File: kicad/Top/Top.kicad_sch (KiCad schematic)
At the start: 0 parts

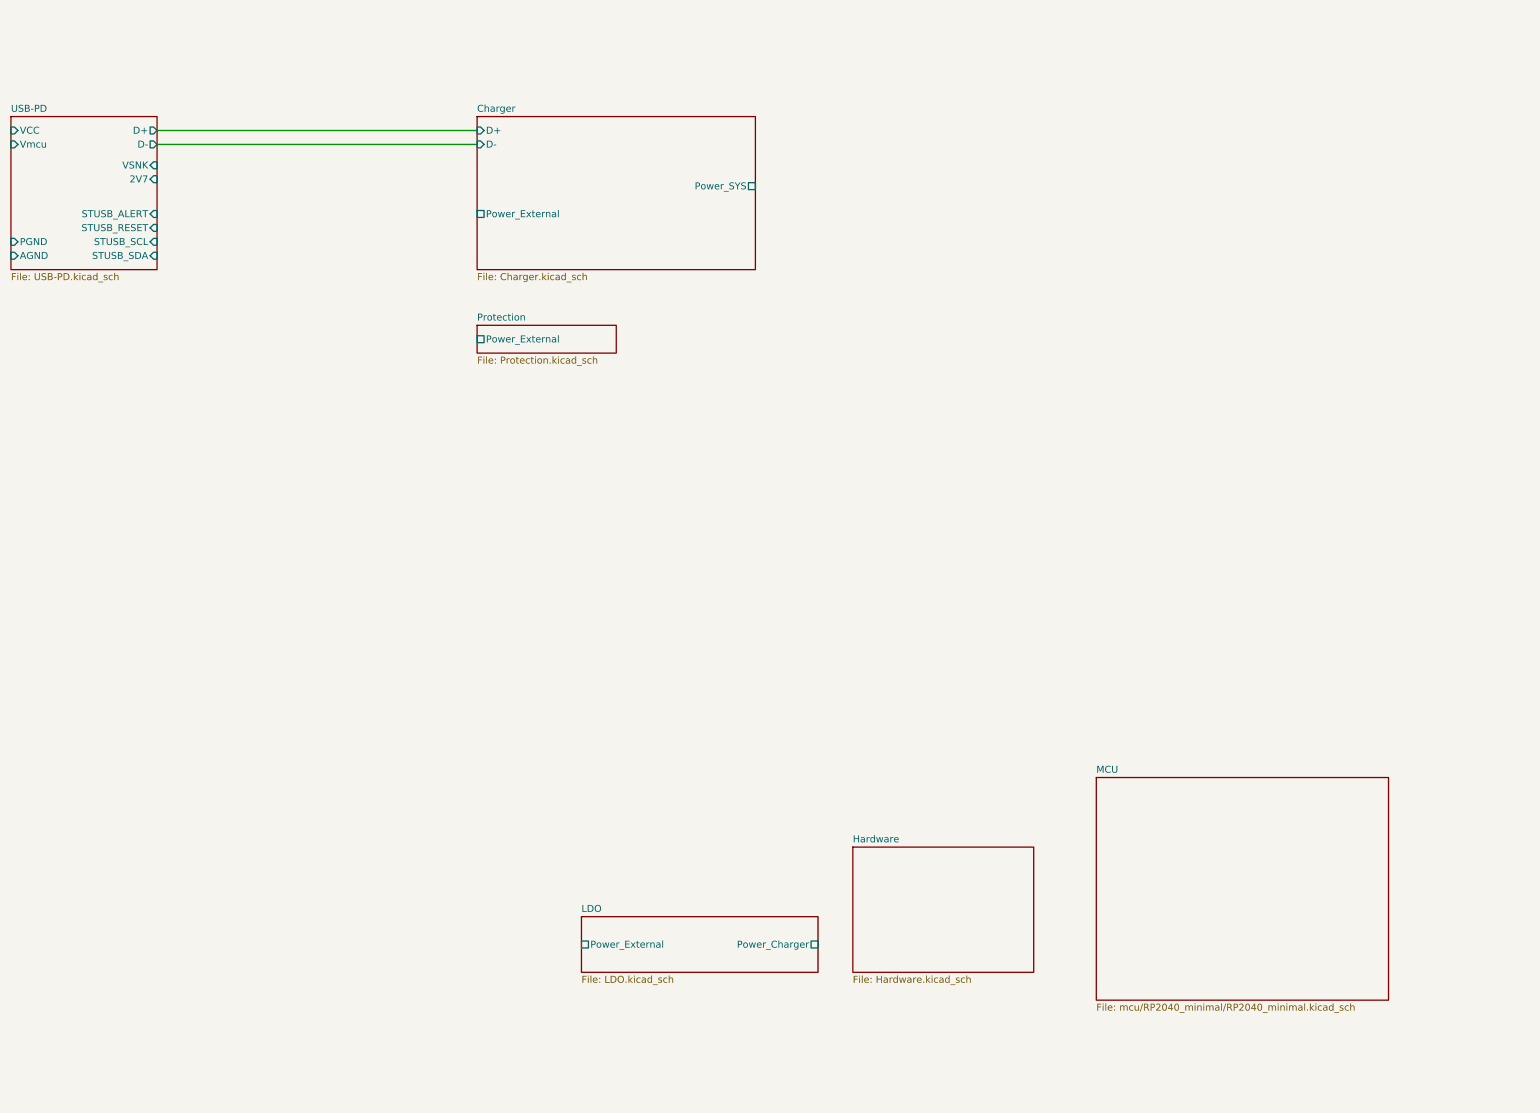
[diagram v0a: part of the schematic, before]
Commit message: Added hierarchial pins to mcu
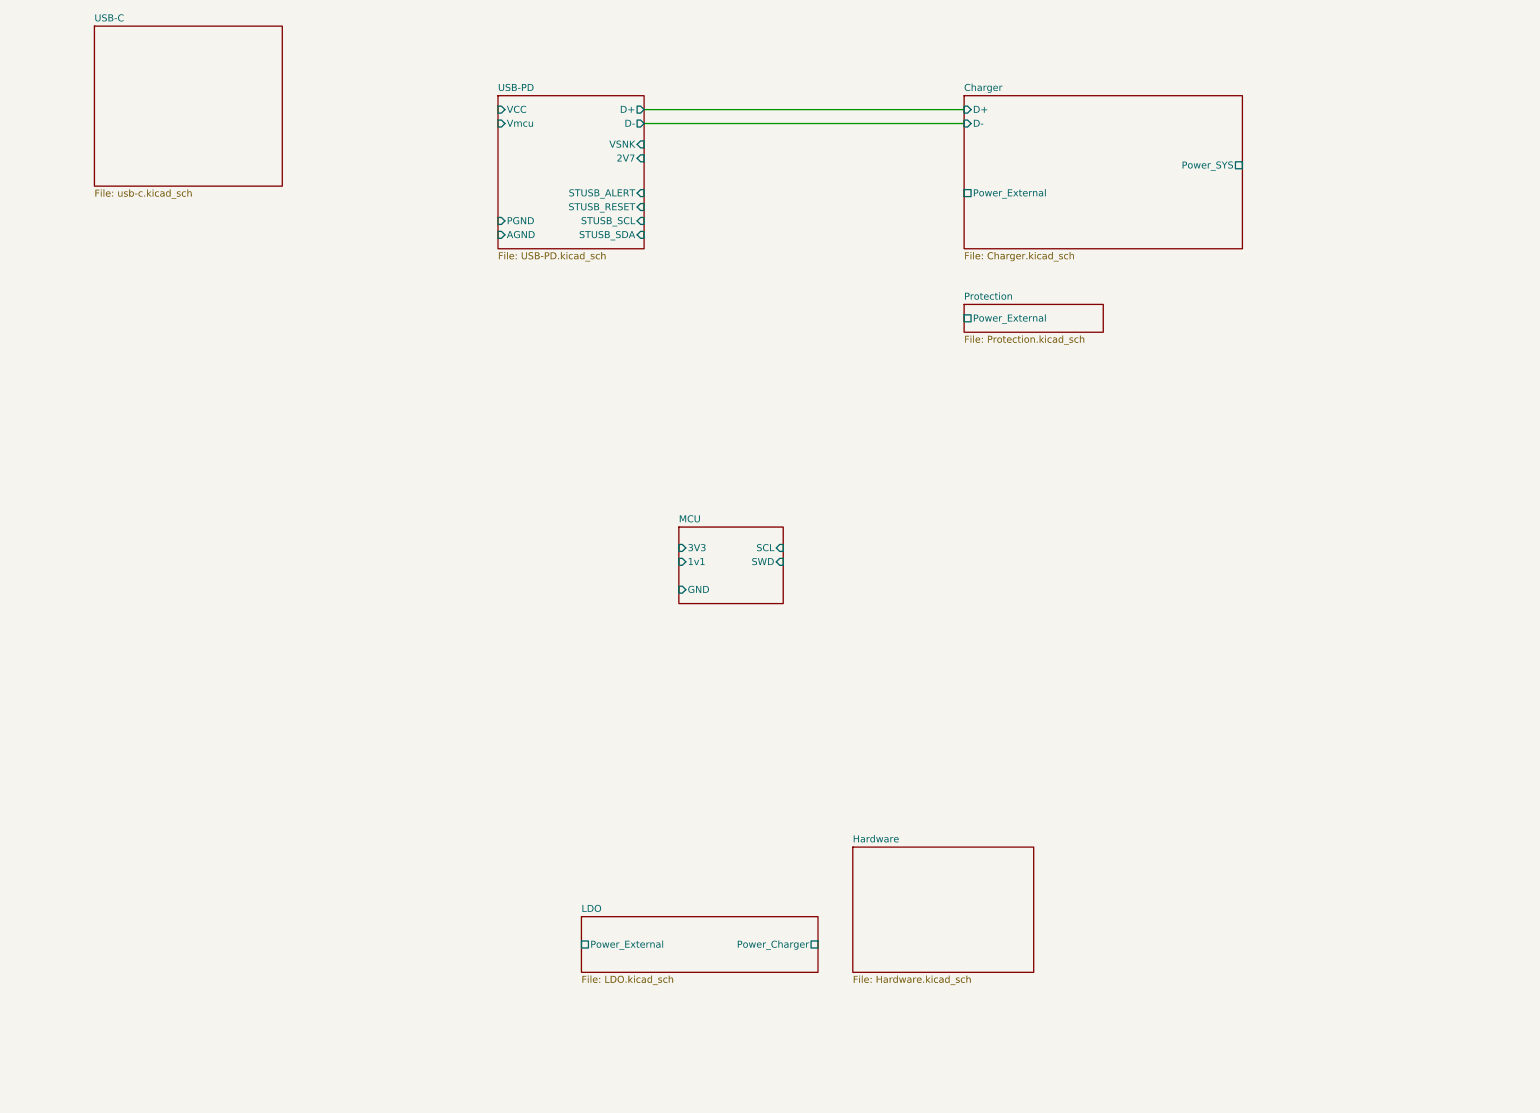
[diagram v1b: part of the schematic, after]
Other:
- added sheet USB-C (usb-c.kicad_sch)
- sheet MCU ports: added 1v1, 3V3, GND, SCL, SWD; removed none

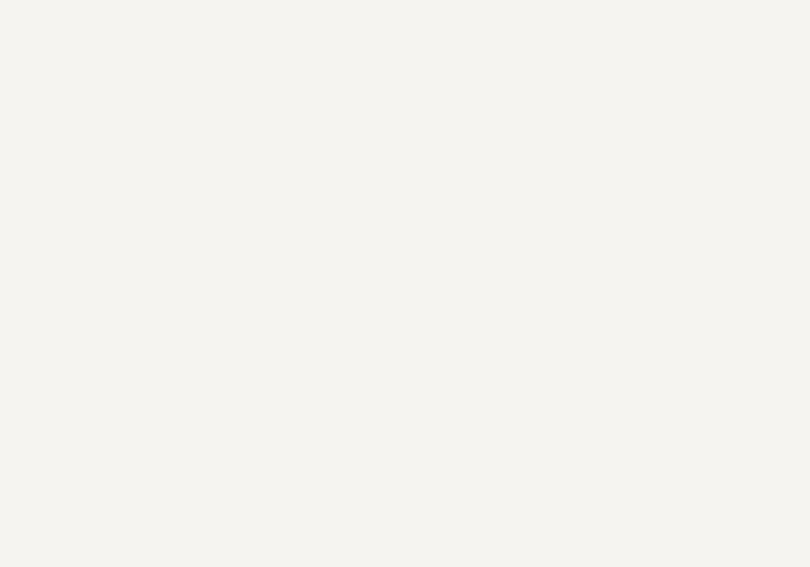
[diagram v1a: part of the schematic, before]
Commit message: Added power mux sheet
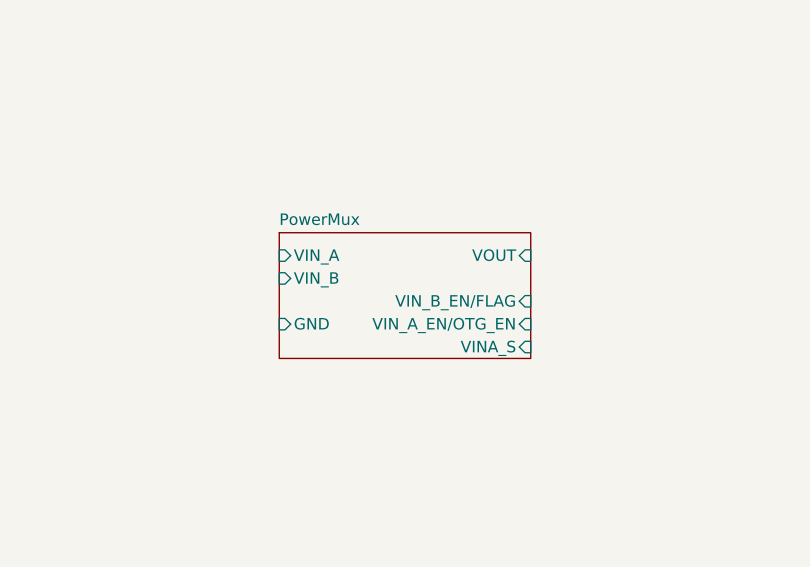
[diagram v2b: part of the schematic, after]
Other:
- added sheet PowerMux (powerMux.kicad_sch)
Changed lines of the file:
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@@
+    )
+  )
+  (sheet (at 58.42 104.14) (size 27.94 13.97) (fields_autoplaced)
+    (stroke (width 0.1524) (type solid) (color 0 0 0 0))
+    (fill (color 0 0 0 0.0000))
+    (property "Sheet name" "PowerMux" (id 0) (at 58.42 103.4284 0)
+      (effects (font (size 1.27 1.27)) (justify left bottom))
+    )
+    (property "Sheet file" "powerMux.kicad_sch" (id 1) (at 58.42 118.6946 0)
+      (effects (font (size 1.27 1.27)) (justify left top) hide)
+    )
+    (pin "VIN_A" input (at 58.42 106.68 180)
+      (effects (font (size 1.27 1.27)) (justify left))
+    )
+    (pin "VIN_B" input (at 58.42 109.22 180)
+      (effects (font (size 1.27 1.27)) (justify left))
+    )
+    (pin "GND" input (at 58.42 114.3 180)
+      (effects (font (size 1.27 1.27)) (justify left))
+    )
+    (pin "VOUT" input (at 86.36 106.68 0)
+      (effects (font (size 1.27 1.27)) (justify right))
+    )
+    (pin "VIN_B_EN{slash}FLAG" input (at 86.36 111.76 0)
+      (effects (font (size 1.27 1.27)) (justify right))
+    )
+    (pin "VIN_A_EN{slash}OTG_EN" input (at 86.36 114.3 0)
+      (effects (font (size 1.27 1.27)) (justify right))
+    )
+    (pin "VINA_S" input (at 86.36 116.84 0)
+      (effects (font (size 1.27 1.27)) (justify right))
     )
   )
@@
     (path "/3b094808-5035-436e-9542-e9e286dde93f" (page "2"))
     (path "/682bfd9a-06ea-4239-a569-efb470bd2019" (page "8"))
+    (path "/e17fda7c-211f-4188-9d42-b948f78009dd" (page "9"))
     (path "/b17a9dbb-4562-473a-b13f-bbad723355f8" (page "11"))
     (path "/3fab603d-ed65-41bd-8de1-51639e39cb06" (page "#"))
@@
       (reference "C?") (unit 1) (value "2.2uF") (footprint "")
     )
+    (path "/e17fda7c-211f-4188-9d42-b948f78009dd/1f468384-5e51-4e4b-afa6-0236cb8d1093"
+      (reference "C?") (unit 1) (value "4.7uF") (footprint "")
+    )
     (path "/682bfd9a-06ea-4239-a569-efb470bd2019/68bc63b2-bef6-4541-a557-67ecebeda82a"
       (reference "C?") (unit 1) (value "100uF") (footprint "")
@@
       (reference "C?") (unit 1) (value "27pF") (footprint "")
     )
+    (path "/e17fda7c-211f-4188-9d42-b948f78009dd/9893cb48-85d5-4f9d-8fce-bbc9116c8ca8"
+      (reference "C?") (unit 1) (value "1uF") (footprint "")
+    )
+    (path "/e17fda7c-211f-4188-9d42-b948f78009dd/bd3fa1b2-2c5c-4953-a19c-e25185455cd8"
+      (reference "C?") (unit 1) (value "1uF") (footprint "")
+    )
     (path "/682bfd9a-06ea-4239-a569-efb470bd2019/f75960c2-547b-4fcf-b700-6e1f788767ff"
       (reference "C?") (unit 1) (value "27pF") (footprint "")
@@
       (reference "U?") (unit 1) (value "STUSB4500QTR") (footprint "Ultra_Librarian:QFN24EP_4X4_STM")
     )
+    (path "/e17fda7c-211f-4188-9d42-b948f78009dd/f92128d7-4486-4481-92d5-2f7afc595dd6"
+      (reference "U?") (unit 1) (value "NCP3901") (footprint "")
+    )
     (path "/b17a9dbb-4562-473a-b13f-bbad723355f8/00000000-0000-0000-0000-00005f0dd35c"

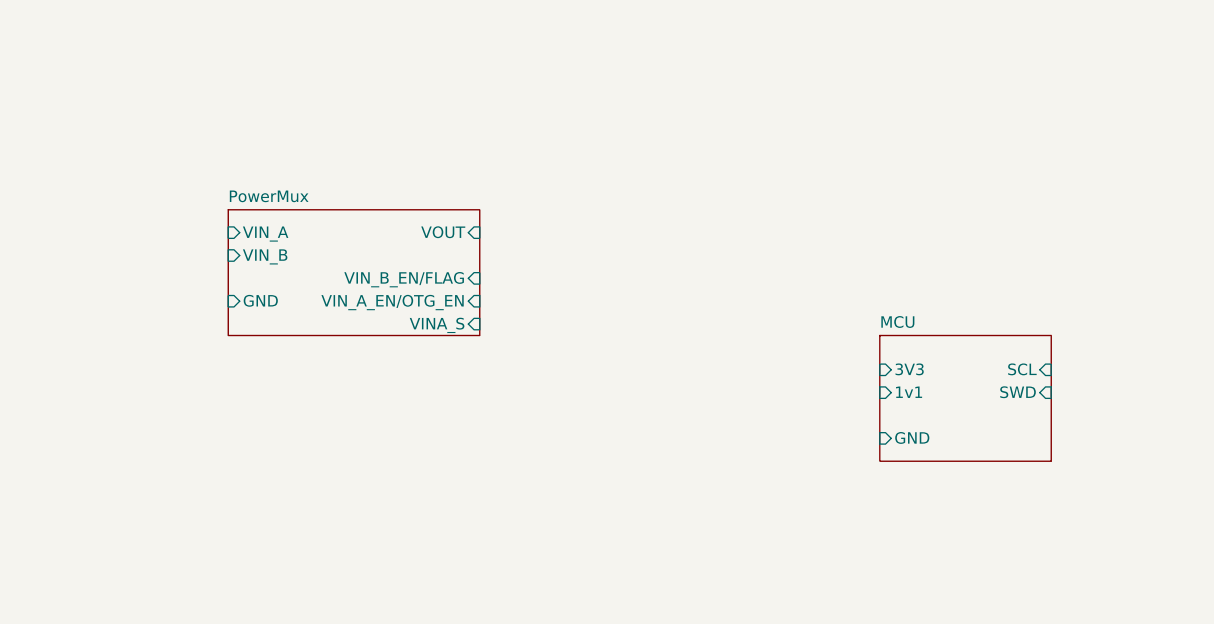
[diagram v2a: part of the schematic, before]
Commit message: Wired up MCU to PowerMux
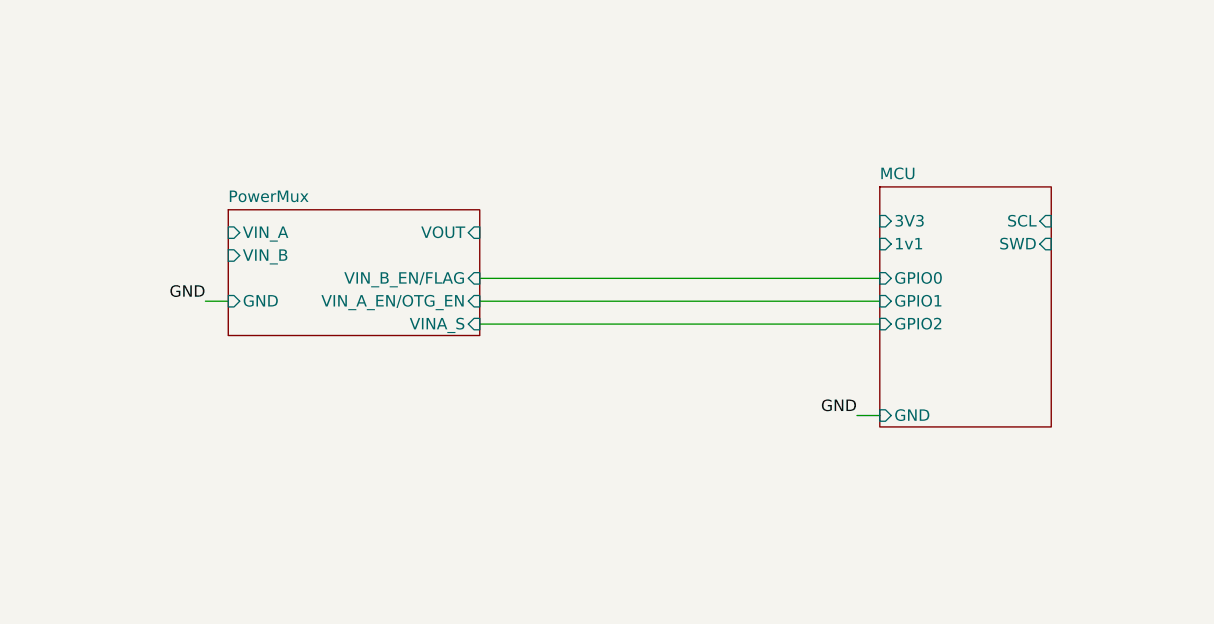
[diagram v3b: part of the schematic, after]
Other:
- sheet MCU ports: added GPIO0, GPIO1, GPIO2; removed none
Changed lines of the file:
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@@
     (stroke (width 0.254) (type default) (color 0 0 0 0))
+  )
+  (wire (pts (xy 86.36 116.84) (xy 130.81 116.84))
+    (stroke (width 0) (type default) (color 0 0 0 0))
+  )
+  (wire (pts (xy 128.27 127) (xy 130.81 127))
+    (stroke (width 0) (type default) (color 0 0 0 0))
+  )
+  (wire (pts (xy 86.36 114.3) (xy 130.81 114.3))
+    (stroke (width 0) (type default) (color 0 0 0 0))
+  )
+  (wire (pts (xy 55.88 114.3) (xy 58.42 114.3))
+    (stroke (width 0) (type default) (color 0 0 0 0))
+  )
+  (wire (pts (xy 86.36 111.76) (xy 130.81 111.76))
+    (stroke (width 0) (type default) (color 0 0 0 0))
   )
   (wire (pts (xy 511.81 340.36) (xy 560.07 340.36))
@@
   (wire (pts (xy 182.88 44.45) (xy 124.46 44.45))
     (stroke (width 0.254) (type default) (color 0 0 0 0))
+  )
+  (label "GND" (at 128.27 127 180)
+    (effects (font (size 1.27 1.27)) (justify right bottom))
+  )
+  (label "GND" (at 55.88 114.3 180)
+    (effects (font (size 1.27 1.27)) (justify right bottom))
   )
   (sheet (at 113.03 189.23) (size 43.18 10.16) (fields_autoplaced)
@@
     )
   )
-  (sheet (at 130.81 118.11) (size 19.05 13.97) (fields_autoplaced)
+  (sheet (at 130.81 101.6) (size 19.05 26.67) (fields_autoplaced)
     (stroke (width 0.1524) (type solid) (color 0 0 0 0))
     (fill (color 0 0 0 0.0000))
-    (property "Sheet name" "MCU" (id 0) (at 130.81 117.3984 0)
+    (property "Sheet name" "MCU" (id 0) (at 130.81 100.8884 0)
       (effects (font (size 1.27 1.27)) (justify left bottom))
     )
-    (property "Sheet file" "mcu/RP2040_minimal/RP2040_minimal.kicad_sch" (id 1) (at 130.81 132.6646 0)
+    (property "Sheet file" "mcu/RP2040_minimal/RP2040_minimal.kicad_sch" (id 1) (at 130.81 128.8546 0)
       (effects (font (size 1.27 1.27)) (justify left top) hide)
     )
-    (pin "3V3" input (at 130.81 121.92 180)
+    (pin "3V3" input (at 130.81 105.41 180)
       (effects (font (size 1.27 1.27)) (justify left))
     )
-    (pin "GND" input (at 130.81 129.54 180)
+    (pin "GND" input (at 130.81 127 180)
       (effects (font (size 1.27 1.27)) (justify left))
     )
-    (pin "1v1" input (at 130.81 124.46 180)
+    (pin "1v1" input (at 130.81 107.95 180)
       (effects (font (size 1.27 1.27)) (justify left))
     )
-    (pin "SCL" input (at 149.86 121.92 0)
+    (pin "SCL" input (at 149.86 105.41 0)
       (effects (font (size 1.27 1.27)) (justify right))
     )
-    (pin "SWD" input (at 149.86 124.46 0)
+    (pin "SWD" input (at 149.86 107.95 0)
       (effects (font (size 1.27 1.27)) (justify right))
     )
+    (pin "GPIO0" input (at 130.81 111.76 180)
+      (effects (font (size 1.27 1.27)) (justify left))
+    )
+    (pin "GPIO1" input (at 130.81 114.3 180)
+      (effects (font (size 1.27 1.27)) (justify left))
+    )
+    (pin "GPIO2" input (at 130.81 116.84 180)
+      (effects (font (size 1.27 1.27)) (justify left))
+    )
   )
